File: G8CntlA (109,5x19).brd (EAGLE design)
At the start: 19 x 109.5 mm, 24 parts, among them SW1 TL2201

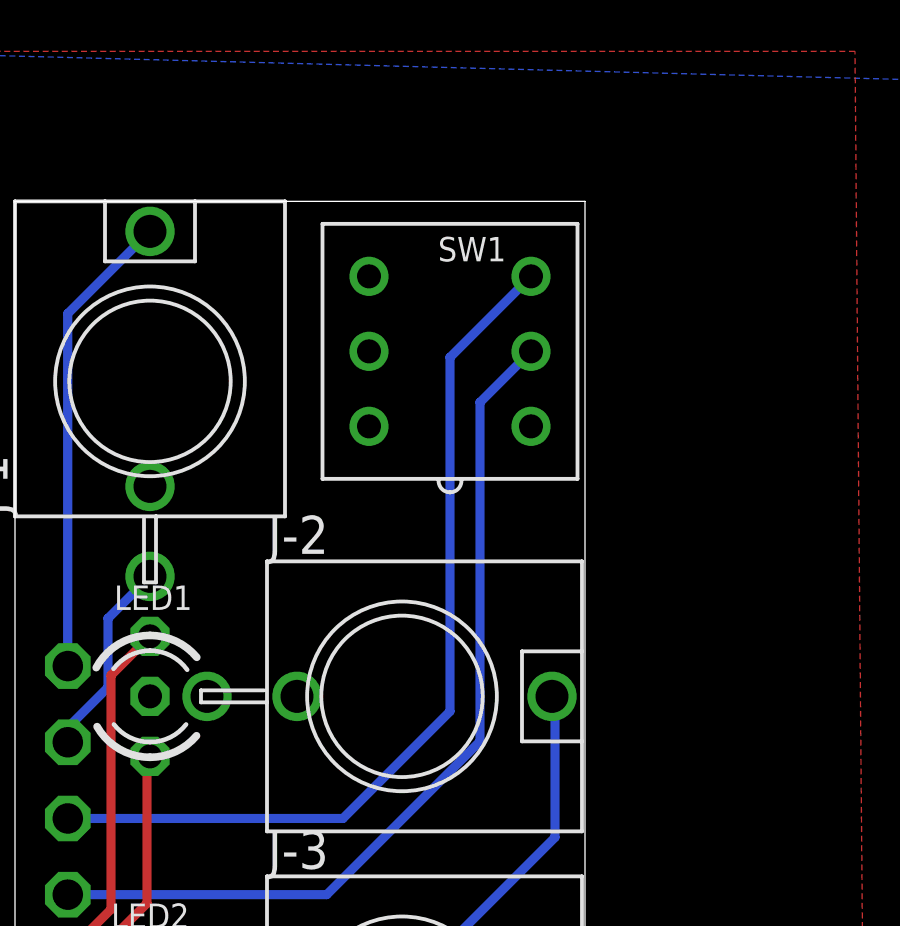
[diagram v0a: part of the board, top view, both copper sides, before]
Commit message: Add files via upload
replaced switch
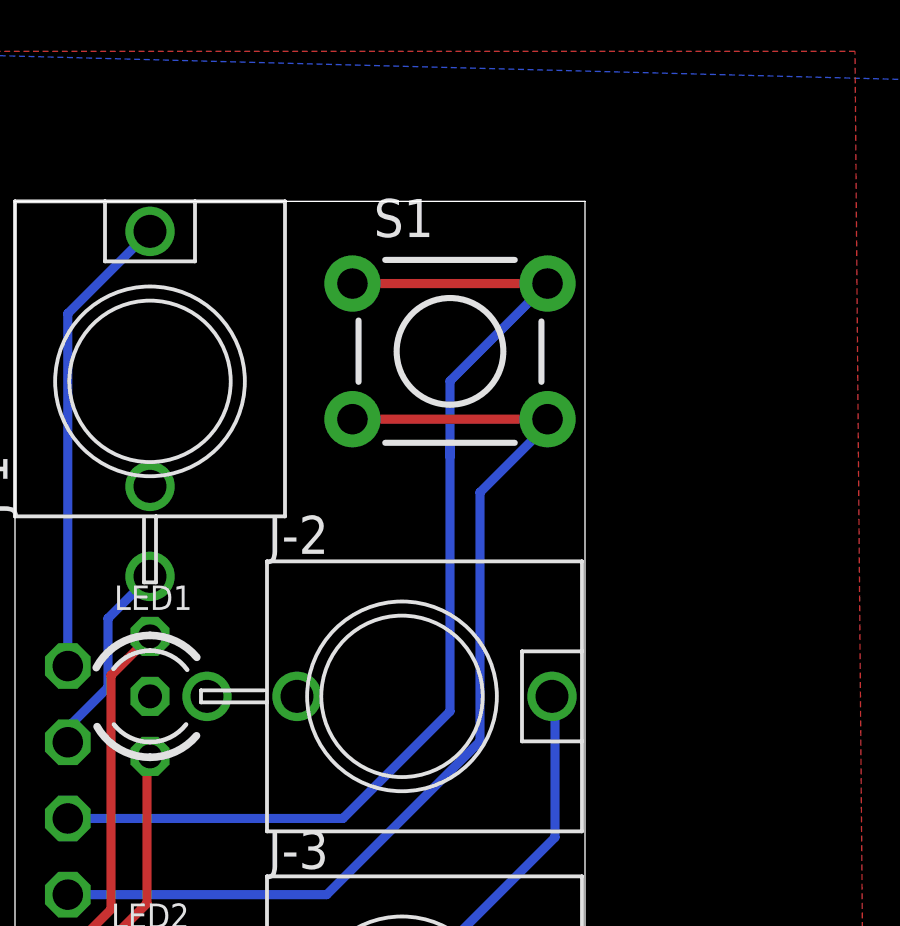
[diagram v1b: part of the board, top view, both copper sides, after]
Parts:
- removed SW1: TL2201, tr-switch:TL2201
- added S1: (no value), !tactile-pth:SPARKFUN_TACTILE-PTH
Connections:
- net N$1: now also S1.1, S1.2; no longer SW1.NO1
- net N$2: now also S1.3, S1.4; no longer SW1.C1
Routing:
- net N$1: track 29.8 -> 36.6 mm
- net N$2: track 29.6 -> 34.0 mm
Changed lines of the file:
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@@
 <?xml version="1.0" encoding="utf-8"?>
 <!DOCTYPE eagle SYSTEM "eagle.dtd">
-<eagle version="8.3.2">
+<eagle version="9.1.1">
 <drawing>
 <settings>
@@
 <layer number="56" name="wert" color="7" fill="1" visible="no" active="no"/>
 <layer number="57" name="tCAD" color="7" fill="1" visible="no" active="no"/>
+<layer number="88" name="SimResults" color="9" fill="1" visible="no" active="no"/>
+<layer number="89" name="SimProbes" color="9" fill="1" visible="no" active="no"/>
 <layer number="90" name="Modules" color="7" fill="1" visible="no" active="no"/>
 <layer number="91" name="Nets" color="2" fill="1" visible="no" active="no"/>
@@
 <param name="dpMaxLengthDifference" value="10mm"/>
 <param name="dpGapFactor" value="2.5"/>
-<param name="checkGrid" value="0"/>
 <param name="checkAngle" value="0"/>
 <param name="checkFont" value="1"/>
 <param name="checkRestrict" value="1"/>
+<param name="checkStop" value="0"/>
+<param name="checkValues" value="0"/>
+<param name="checkNames" value="1"/>
+<param name="checkWireStubs" value="1"/>
+<param name="checkPolygonWidth" value="0"/>
 <param name="useDiameter" value="13"/>
 <param name="maxErrors" value="50"/>
@@
 <attribute name="VALUE" x="6.405" y="17.849" size="1.27" layer="27" ratio="10"/>
 </element>
-<element name="SW1" library="tr-switch" package="TL2201" value="TL2201" x="14.5" y="104.5" smashed="yes" rot="R90">
-<attribute name="NAME" x="14.1" y="107.5" size="0.8128" layer="25" font="vector" ratio="12"/>
-<attribute name="VALUE" x="20.5" y="101.5" size="1.016" layer="27" font="vector" ratio="12" rot="R90"/>
-</element>
 <element name="SV1" library="tr-con" package="MA08-OCT" value="" x="1.76" y="85.12" smashed="yes" rot="MR270">
 <attribute name="NAME" x="2.78" y="95.491" size="0.8128" layer="26" font="vector" ratio="12" rot="MR0"/>
@@
 <element name="J-1" library="!MusicThingModular" package="WQP-PJ301M-12_JACK" value="THONKICONNNEW" x="4.5" y="103.5"/>
 <element name="J-2" library="!MusicThingModular" package="WQP-PJ301M-12_JACK" value="THONKICONNNEW" x="12.9" y="93" rot="R270"/>
+<element name="S1" library="!tactile-pth" package="SPARKFUN_TACTILE-PTH" value="" x="14.5" y="104.5"/>
 </elements>
 <signals>
 <signal name="N$1">
 <contactref element="SV1" pad="3"/>
-<contactref element="SW1" pad="NO1"/>
 <wire x1="1.76" y1="88.93" x2="10.93" y2="88.93" width="0.3048" layer="16"/>
 <wire x1="10.93" y1="88.93" x2="14.5" y2="92.5" width="0.3048" layer="16"/>
-<wire x1="14.5" y1="92.5" x2="14.5" y2="104.3" width="0.3048" layer="16"/>
-<wire x1="14.5" y1="104.3" x2="17.2" y2="107" width="0.3048" layer="16"/>
+<wire x1="14.5" y1="92.5" x2="14.5" y2="101" width="0.3048" layer="16"/>
+<contactref element="S1" pad="2"/>
+<contactref element="S1" pad="1"/>
+<wire x1="14.5" y1="101" x2="14.5" y2="101.3" width="0.3048" layer="16"/>
+<wire x1="14.5" y1="101" x2="14.5" y2="103.5094" width="0.3048" layer="16"/>
+<wire x1="14.5" y1="103.5094" x2="17.7512" y2="106.7606" width="0.3048" layer="16"/>
+<wire x1="11.2488" y1="106.7606" x2="17.7512" y2="106.7606" width="0.3048" layer="1"/>
 </signal>
 <signal name="N$2">
-<contactref element="SW1" pad="C1"/>
 <contactref element="SV1" pad="4"/>
 <wire x1="1.76" y1="86.39" x2="10.39" y2="86.39" width="0.3048" layer="16"/>
 <wire x1="10.39" y1="86.39" x2="15.5" y2="91.5" width="0.3048" layer="16"/>
-<wire x1="15.5" y1="91.5" x2="15.5" y2="102.8" width="0.3048" layer="16"/>
-<wire x1="15.5" y1="102.8" x2="17.2" y2="104.5" width="0.3048" layer="16"/>
+<wire x1="15.5" y1="91.5" x2="15.5" y2="99.8" width="0.3048" layer="16"/>
+<contactref element="S1" pad="4"/>
+<contactref element="S1" pad="3"/>
+<wire x1="15.5" y1="99.8" x2="17.7512" y2="102.0512" width="0.3048" layer="16"/>
+<wire x1="17.7512" y1="102.0512" x2="17.7512" y2="102.2394" width="0.3048" layer="16"/>
+<wire x1="11.2488" y1="102.2394" x2="17.7512" y2="102.2394" width="0.3048" layer="1"/>
 </signal>
 <signal name="N$4">
@@
 </signal>
 </signals>
+<mfgpreviewcolors>
+<mfgpreviewcolor name="soldermaskcolor" color="0xC8008000"/>
+<mfgpreviewcolor name="silkscreencolor" color="0xFFFEFEFE"/>
+<mfgpreviewcolor name="backgroundcolor" color="0xFF282828"/>
+<mfgpreviewcolor name="coppercolor" color="0xFFFFBF00"/>
+<mfgpreviewcolor name="substratecolor" color="0xFF786E46"/>
+</mfgpreviewcolors>
 </board>
 </drawing>
